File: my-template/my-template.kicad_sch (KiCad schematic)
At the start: 23 parts, among them J1 1054500101, J5 10x1mm FFC/FPC, U1 ESP32-S3-WROOM-1-N16R8, U2 MCP1825S-2502E/DB

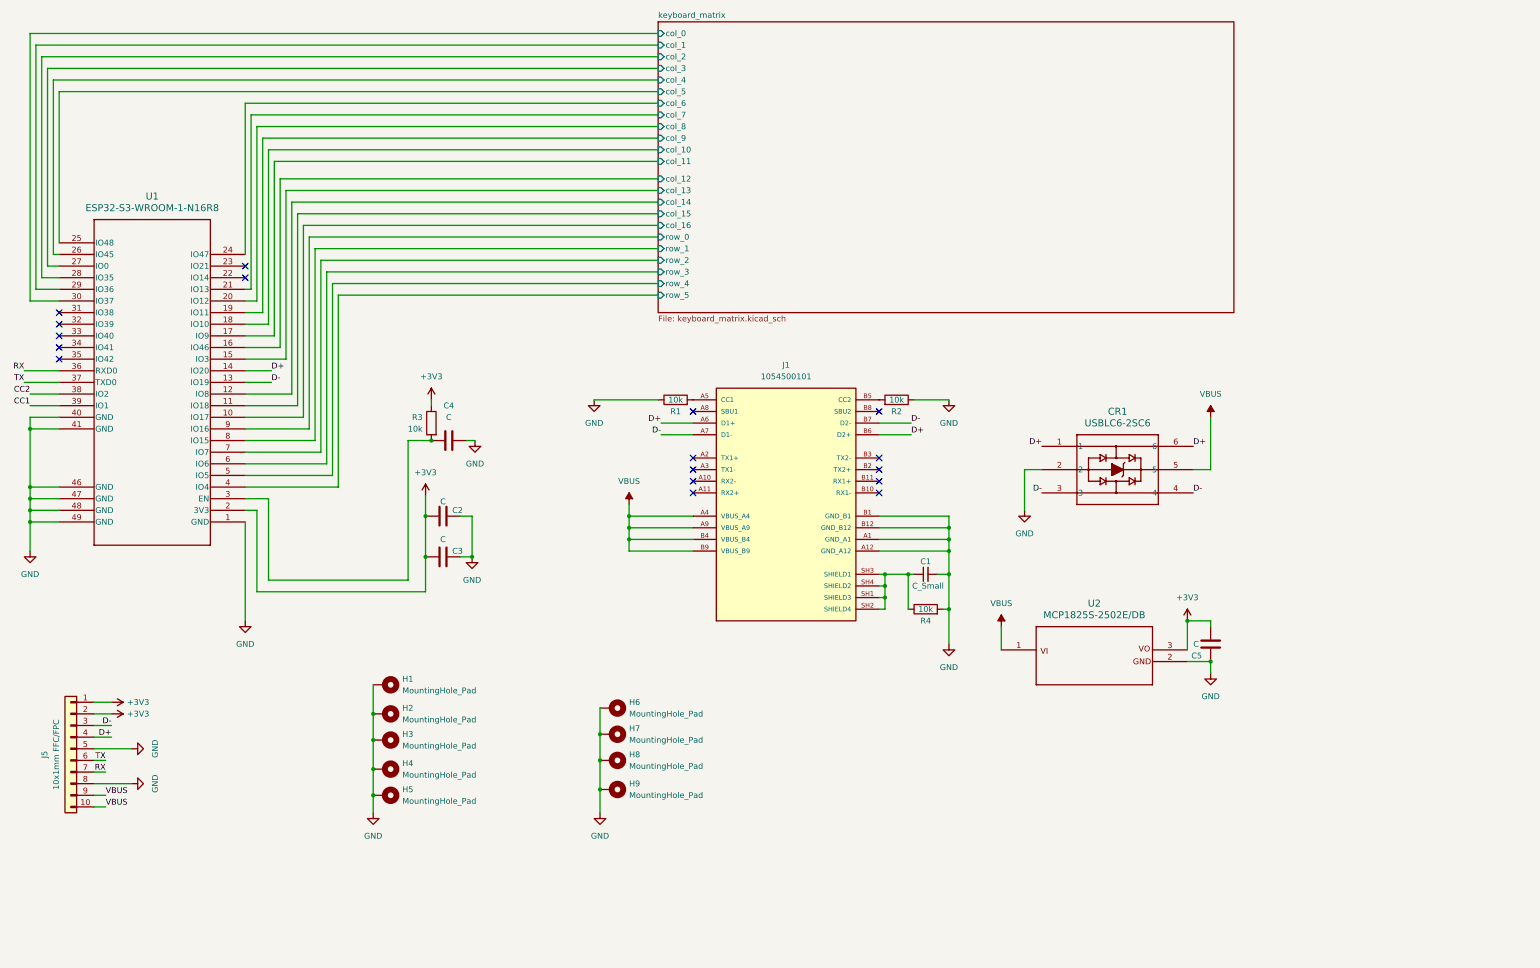
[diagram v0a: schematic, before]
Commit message: lipo schematic done
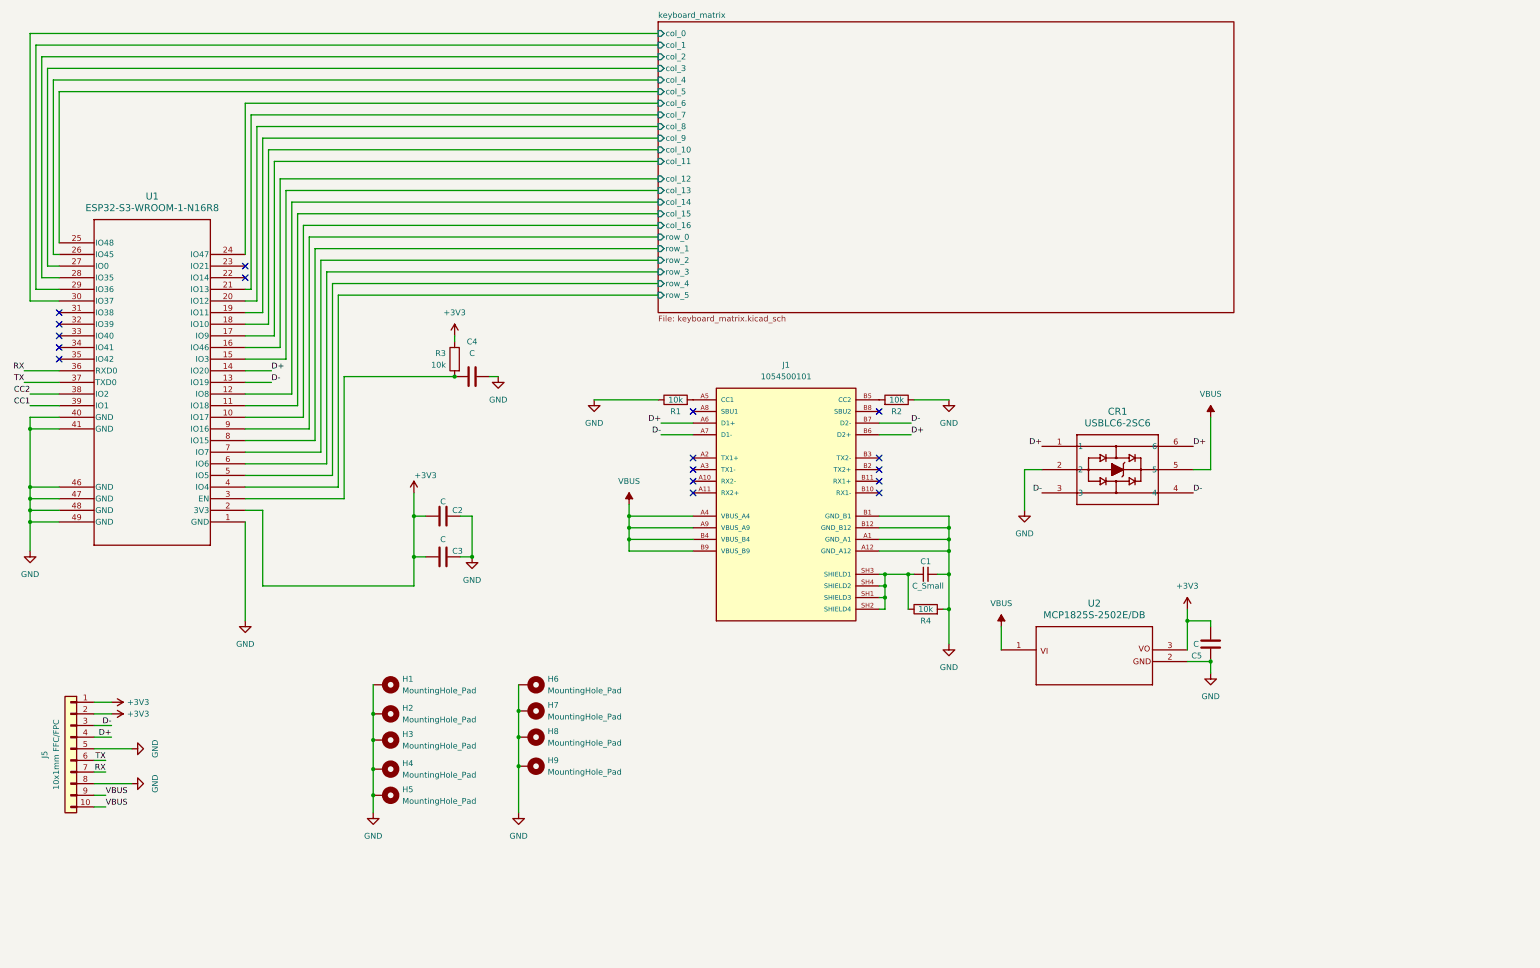
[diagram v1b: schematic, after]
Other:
- title: (none) -> Tenkeyless Keyboard
- moved on the sheet: C4, H6, H7, H8, H9, R3

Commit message: resolved warnings in esp circuit
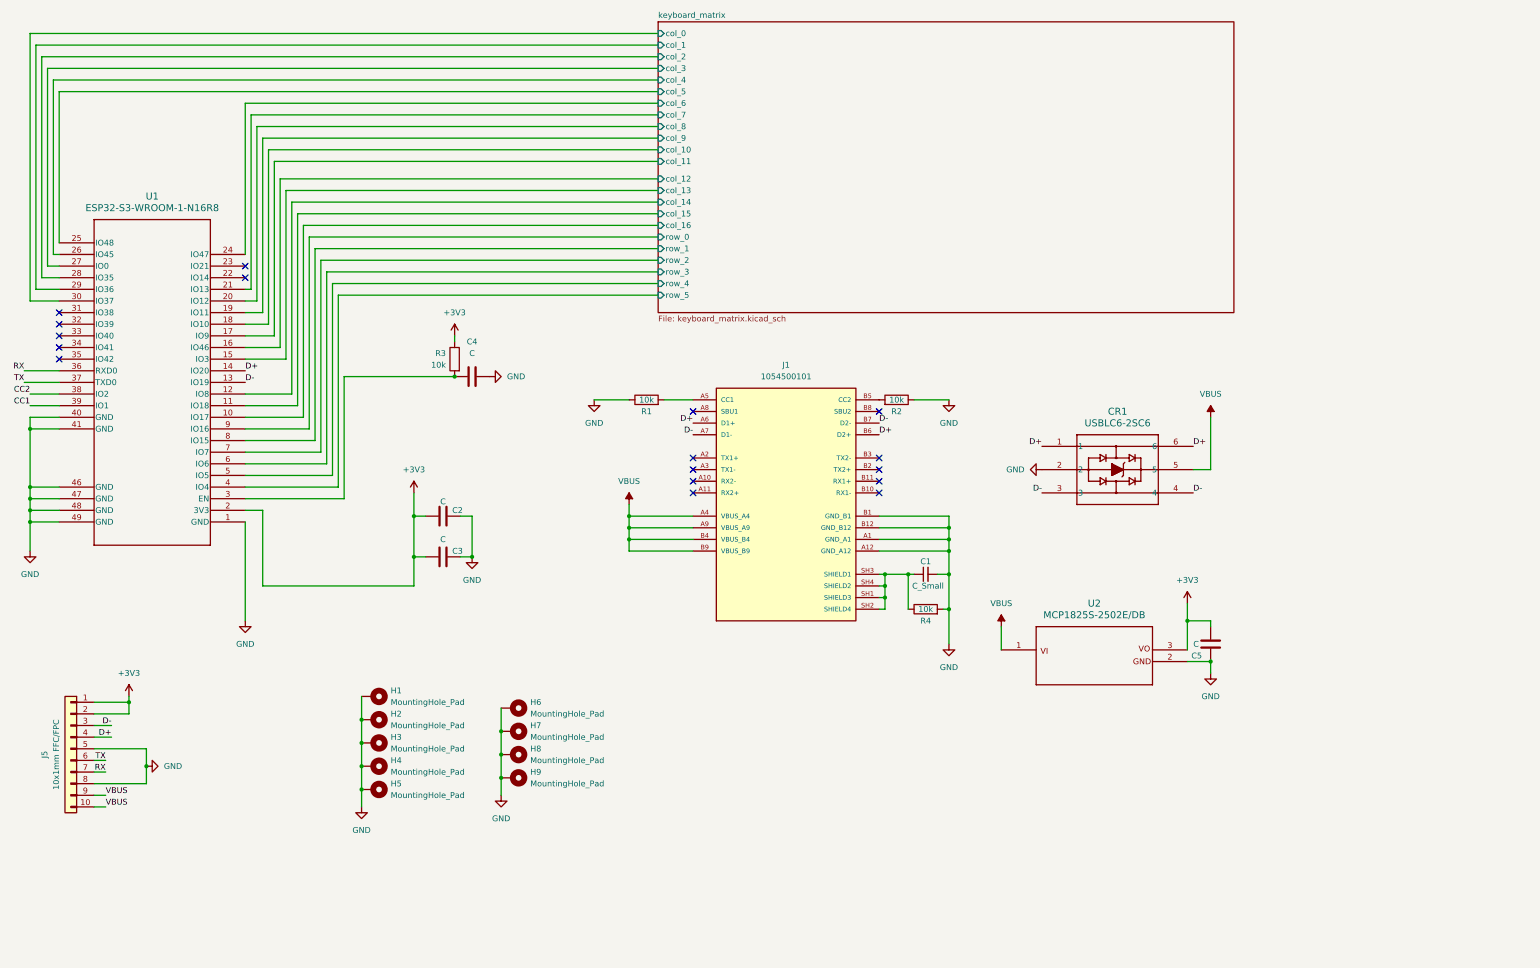
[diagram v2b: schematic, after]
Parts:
- H1, H2, H3, H4, H5, H6, H7, H8, H9: now left out of the parts list
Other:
- moved on the sheet: R1

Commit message: component placement done
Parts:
- added J2: BOOT, Connector_PinHeader_2.54mm:PinHeader_1x02_P2.54mm_Horizontal, symbol Connector:Conn_01x02_Pin
- added R5: 10K, Resistor_SMD:R_0603_1608Metric, symbol Device:R_Small
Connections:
- net +3V3: now also R5.1
- net CC1: now also J1.A5 (CC1), R1.2
- net CC2: now also J1.B5 (CC2), R2.2
- net GND: now also J2.1 (Pin_1)
- net keyboard_matrix/col_3: now also U1.31 (IO38); no longer U1.27 (IO0)
- new net: J2.2 (Pin_2), R5.2, U1.27 (IO0)
- no-connect marks 17 -> 16
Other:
- moved on the sheet: C1, C2, C3, C4, C5, CR1, H1, H2, H3, H4, H5, H6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
